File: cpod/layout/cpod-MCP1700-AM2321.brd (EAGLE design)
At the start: 15 parts, among them IC1 PCF8563DIP, Y1 32.768kHz

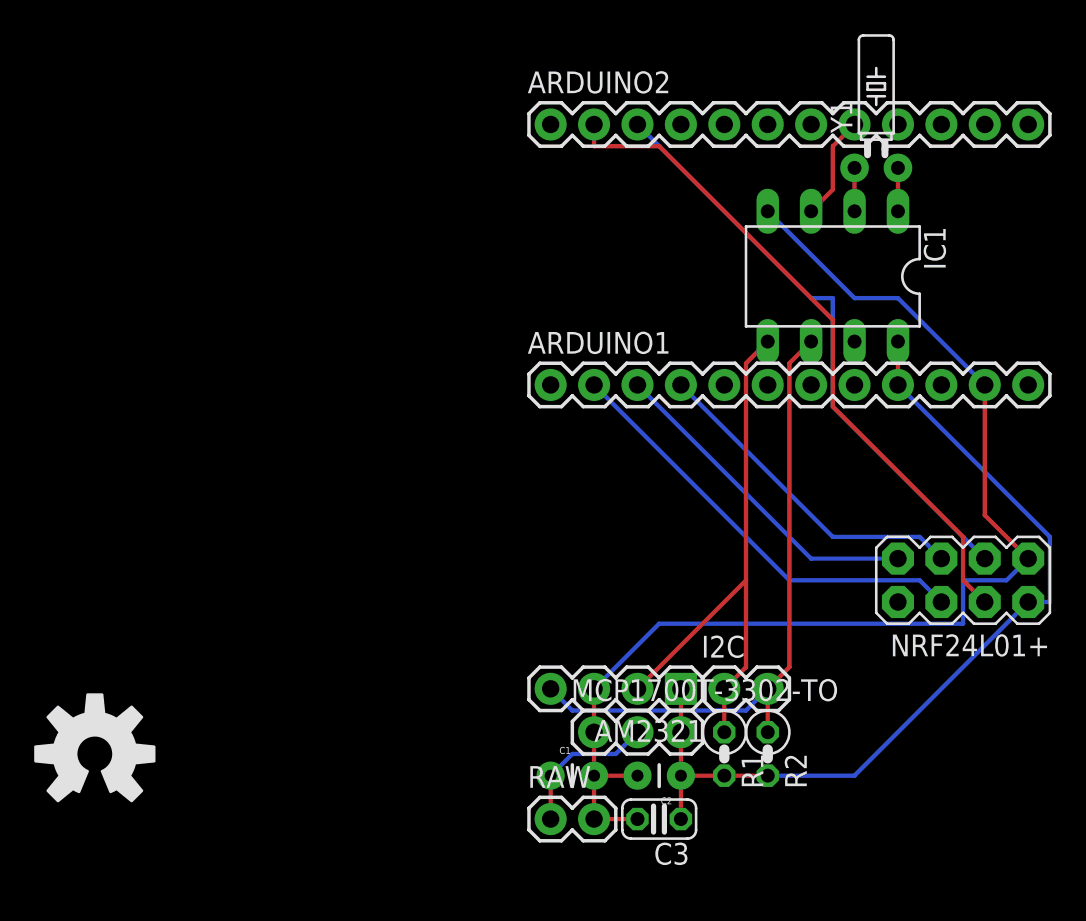
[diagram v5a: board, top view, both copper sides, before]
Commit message: 增加INT0的上拉电阻
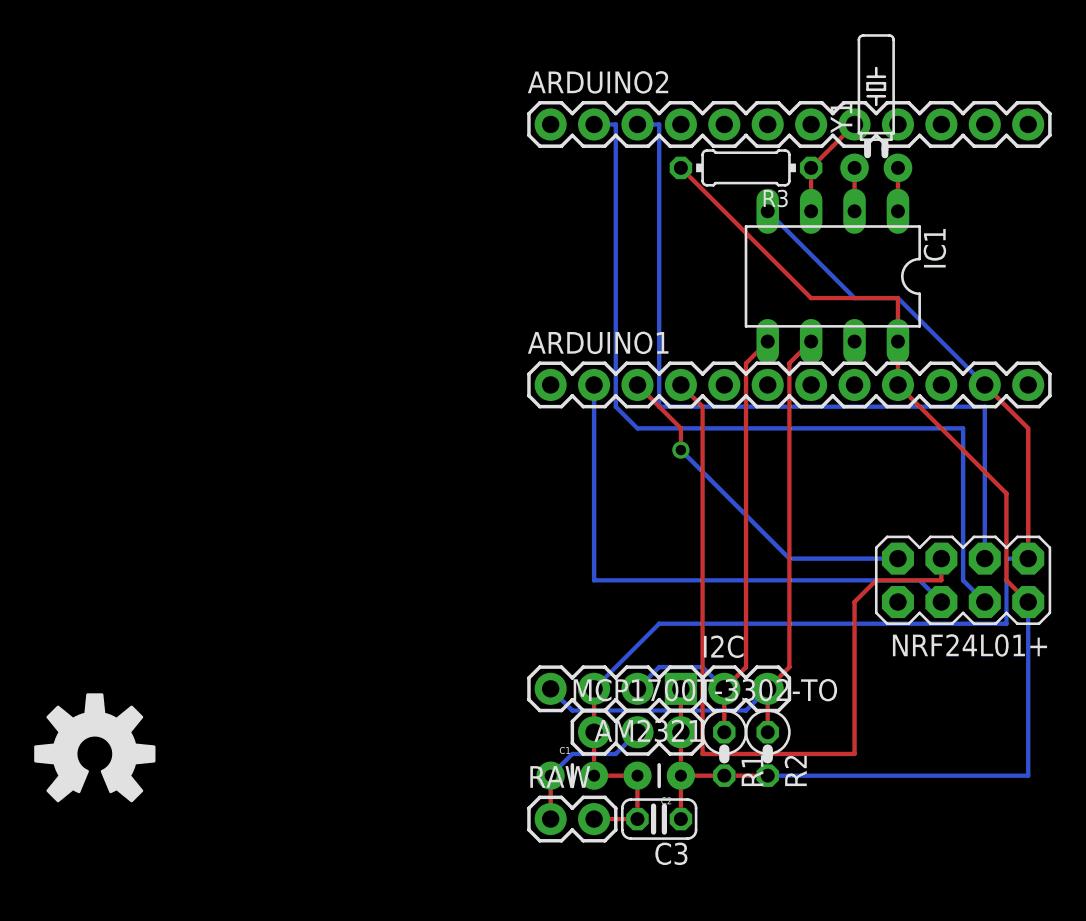
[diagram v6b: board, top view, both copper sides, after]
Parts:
- added R3: 5.1k, rcl:0204/7
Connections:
- net INT0: now also R3.1
- net VCC: now also R3.2
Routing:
- net SCK: track 19.4 -> 46.8 mm
- net VCC: track 52.3 -> 74.9 mm
- net CE: track 34.6 -> 45.7 mm
- net CSN: track 39.6 -> 49.3 mm
- net MOSI: track 25.6 -> 32.3 mm
- net SDA: track 32.9 -> 30.0 mm
- net MISO: track 19.4 -> 20.2 mm, vias 0 -> 1
- net GND: track 70.9 -> 71.6 mm
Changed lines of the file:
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@@
 <element name="Y1" library="SparkFun-FreqCtrl" package="TC26H" value="32.768kHz" x="50.8" y="-3.81"/>
 <element name="C3" library="rcl" package="C025-024X044" value="100nF" x="38.1" y="-41.91" rot="R180"/>
+<element name="R3" library="rcl" package="0204/7" value="5.1k" x="43.18" y="-3.81" rot="R180"/>
 </elements>
 <signals>
@@
 <contactref element="IC1" pad="4"/>
 <contactref element="ARDUINO1" pad="11"/>
+<contactref element="C2" pad="2"/>
+<contactref element="C3" pad="2"/>
+<wire x1="34.29" y1="-41.91" x2="36.83" y2="-41.91" width="0.254" layer="1"/>
 <wire x1="34.29" y1="-36.83" x2="34.29" y2="-39.37" width="0.254" layer="1"/>
-<wire x1="34.29" y1="-39.37" x2="34.29" y2="-41.91" width="0.254" layer="1"/>
+<wire x1="34.29" y1="-39.37" x2="36.83" y2="-39.37" width="0.254" layer="1"/>
 <wire x1="34.29" y1="-36.83" x2="34.29" y2="-34.29" width="0.254" layer="1"/>
+<wire x1="36.83" y1="-39.37" x2="36.83" y2="-41.91" width="0.254" layer="1"/>
 <wire x1="49.53" y1="-11.43" x2="44.45" y2="-6.35" width="0.254" layer="16"/>
 <wire x1="52.07" y1="-11.43" x2="49.53" y2="-11.43" width="0.254" layer="16"/>
 <wire x1="57.15" y1="-16.51" x2="52.07" y2="-11.43" width="0.254" layer="16"/>
-<wire x1="57.15" y1="-24.13" x2="59.69" y2="-26.67" width="0.254" layer="1"/>
-<wire x1="57.15" y1="-16.51" x2="57.15" y2="-24.13" width="0.254" layer="1"/>
+<wire x1="59.69" y1="-19.05" x2="59.69" y2="-26.67" width="0.254" layer="1"/>
+<wire x1="57.15" y1="-16.51" x2="59.69" y2="-19.05" width="0.254" layer="1"/>
 <wire x1="38.1" y1="-30.48" x2="34.29" y2="-34.29" width="0.254" layer="16"/>
-<wire x1="55.88" y1="-30.48" x2="38.1" y2="-30.48" width="0.254" layer="16"/>
-<wire x1="55.88" y1="-27.94" x2="55.88" y2="-30.48" width="0.254" layer="16"/>
-<wire x1="58.42" y1="-27.94" x2="55.88" y2="-27.94" width="0.254" layer="16"/>
-<wire x1="59.69" y1="-26.67" x2="58.42" y2="-27.94" width="0.254" layer="16"/>
-<contactref element="C2" pad="2"/>
-<contactref element="C3" pad="2"/>
-<wire x1="34.29" y1="-41.91" x2="36.83" y2="-41.91" width="0.254" layer="1"/>
-<wire x1="36.83" y1="-39.37" x2="34.29" y2="-39.37" width="0.254" layer="1"/>
+<wire x1="58.42" y1="-30.48" x2="38.1" y2="-30.48" width="0.254" layer="16"/>
+<wire x1="58.42" y1="-26.67" x2="58.42" y2="-30.48" width="0.254" layer="16"/>
+<wire x1="59.69" y1="-26.67" x2="58.42" y2="-26.67" width="0.254" layer="16"/>
 </signal>
 <signal name="SDA">
@@
 <wire x1="41.91" y1="-34.29" x2="41.91" y2="-36.83" width="0.254" layer="1"/>
 <wire x1="43.18" y1="-15.24" x2="44.45" y2="-13.97" width="0.254" layer="1"/>
-<wire x1="43.18" y1="-33.02" x2="43.18" y2="-27.94" width="0.254" layer="1"/>
-<wire x1="43.18" y1="-27.94" x2="43.18" y2="-15.24" width="0.254" layer="1"/>
+<wire x1="43.18" y1="-33.02" x2="43.18" y2="-15.24" width="0.254" layer="1"/>
 <wire x1="41.91" y1="-34.29" x2="43.18" y2="-33.02" width="0.254" layer="1"/>
-<wire x1="43.18" y1="-27.94" x2="36.83" y2="-34.29" width="0.254" layer="1"/>
+<wire x1="38.1" y1="-33.02" x2="36.83" y2="-34.29" width="0.254" layer="16"/>
+<wire x1="40.64" y1="-33.02" x2="38.1" y2="-33.02" width="0.254" layer="16"/>
+<wire x1="41.91" y1="-34.29" x2="40.64" y2="-33.02" width="0.254" layer="16"/>
 </signal>
 <signal name="VCC">
@@
 <contactref element="MCP1700T-3302-TO" pad="3"/>
 <contactref element="IC1" pad="8"/>
-<wire x1="39.37" y1="-34.29" x2="39.37" y2="-36.83" width="0.254" layer="1"/>
-<wire x1="52.07" y1="-16.51" x2="52.07" y2="-13.97" width="0.254" layer="1"/>
-<wire x1="41.91" y1="-39.37" x2="44.45" y2="-39.37" width="0.254" layer="1"/>
-<wire x1="49.53" y1="-39.37" x2="59.69" y2="-29.21" width="0.254" layer="16"/>
-<wire x1="44.45" y1="-39.37" x2="49.53" y2="-39.37" width="0.254" layer="16"/>
-<wire x1="60.96" y1="-25.4" x2="52.07" y2="-16.51" width="0.254" layer="16"/>
-<wire x1="60.96" y1="-29.21" x2="60.96" y2="-25.4" width="0.254" layer="16"/>
-<wire x1="59.69" y1="-29.21" x2="60.96" y2="-29.21" width="0.254" layer="16"/>
 <contactref element="C2" pad="1"/>
 <contactref element="C3" pad="1"/>
+<contactref element="R3" pad="2"/>
+<wire x1="46.99" y1="-11.43" x2="39.37" y2="-3.81" width="0.254" layer="1"/>
+<wire x1="52.07" y1="-11.43" x2="46.99" y2="-11.43" width="0.254" layer="1"/>
+<wire x1="52.07" y1="-13.97" x2="52.07" y2="-11.43" width="0.254" layer="1"/>
+<wire x1="52.07" y1="-13.97" x2="52.07" y2="-16.51" width="0.254" layer="1"/>
+<wire x1="39.37" y1="-34.29" x2="39.37" y2="-36.83" width="0.254" layer="1"/>
 <wire x1="39.37" y1="-39.37" x2="39.37" y2="-41.91" width="0.254" layer="1"/>
-<wire x1="39.37" y1="-36.83" x2="39.37" y2="-39.37" width="0.254" layer="1"/>
-<wire x1="41.91" y1="-39.37" x2="39.37" y2="-39.37" width="0.254" layer="1"/>
+<wire x1="39.37" y1="-39.37" x2="41.91" y2="-39.37" width="0.254" layer="1"/>
+<wire x1="41.91" y1="-39.37" x2="44.45" y2="-39.37" width="0.254" layer="1"/>
+<wire x1="59.69" y1="-39.37" x2="59.69" y2="-29.21" width="0.254" layer="16"/>
+<wire x1="44.45" y1="-39.37" x2="59.69" y2="-39.37" width="0.254" layer="16"/>
+<wire x1="39.37" y1="-39.37" x2="39.37" y2="-36.83" width="0.254" layer="1"/>
+<wire x1="58.42" y1="-22.86" x2="52.07" y2="-16.51" width="0.254" layer="1"/>
+<wire x1="58.42" y1="-27.94" x2="58.42" y2="-22.86" width="0.254" layer="1"/>
+<wire x1="59.69" y1="-29.21" x2="58.42" y2="-27.94" width="0.254" layer="1"/>
 </signal>
 <signal name="RAW">
@@
 <contactref element="ARDUINO1" pad="4"/>
 <contactref element="NRF24L01+" pad="5"/>
-<wire x1="48.26" y1="-25.4" x2="39.37" y2="-16.51" width="0.254" layer="16"/>
-<wire x1="53.34" y1="-25.4" x2="48.26" y2="-25.4" width="0.254" layer="16"/>
-<wire x1="54.61" y1="-26.67" x2="53.34" y2="-25.4" width="0.254" layer="16"/>
+<wire x1="40.64" y1="-17.78" x2="39.37" y2="-16.51" width="0.254" layer="1"/>
+<wire x1="40.64" y1="-38.1" x2="40.64" y2="-17.78" width="0.254" layer="1"/>
+<wire x1="49.53" y1="-38.1" x2="40.64" y2="-38.1" width="0.254" layer="1"/>
+<wire x1="49.53" y1="-29.21" x2="49.53" y2="-38.1" width="0.254" layer="1"/>
+<wire x1="50.8" y1="-27.94" x2="49.53" y2="-29.21" width="0.254" layer="1"/>
+<wire x1="54.61" y1="-27.94" x2="50.8" y2="-27.94" width="0.254" layer="1"/>
+<wire x1="54.61" y1="-26.67" x2="54.61" y2="-27.94" width="0.254" layer="1"/>
 </signal>
 <signal name="MISO">
 <contactref element="ARDUINO1" pad="3"/>
 <contactref element="NRF24L01+" pad="7"/>
-<wire x1="46.99" y1="-26.67" x2="36.83" y2="-16.51" width="0.254" layer="16"/>
-<wire x1="52.07" y1="-26.67" x2="46.99" y2="-26.67" width="0.254" layer="16"/>
+<wire x1="39.37" y1="-19.05" x2="36.83" y2="-16.51" width="0.254" layer="1"/>
+<wire x1="39.37" y1="-20.32" x2="39.37" y2="-19.05" width="0.254" layer="1"/>
+<wire x1="45.72" y1="-26.67" x2="39.37" y2="-20.32" width="0.254" layer="16"/>
+<wire x1="52.07" y1="-26.67" x2="45.72" y2="-26.67" width="0.254" layer="16"/>
+<via x="39.37" y="-20.32" extent="1-16" drill="0.6096"/>
 </signal>
 <signal name="MOSI">
 <contactref element="ARDUINO1" pad="2"/>
 <contactref element="NRF24L01+" pad="6"/>
-<wire x1="45.72" y1="-27.94" x2="34.29" y2="-16.51" width="0.254" layer="16"/>
-<wire x1="53.34" y1="-27.94" x2="45.72" y2="-27.94" width="0.254" layer="16"/>
+<wire x1="34.29" y1="-27.94" x2="34.29" y2="-16.51" width="0.254" layer="16"/>
+<wire x1="53.34" y1="-27.94" x2="34.29" y2="-27.94" width="0.254" layer="16"/>
 <wire x1="54.61" y1="-29.21" x2="53.34" y2="-27.94" width="0.254" layer="16"/>
 </signal>
@@
 <contactref element="NRF24L01+" pad="4"/>
 <contactref element="ARDUINO2" pad="2"/>
-<wire x1="55.88" y1="-27.94" x2="57.15" y2="-29.21" width="0.254" layer="1"/>
-<wire x1="55.88" y1="-25.4" x2="55.88" y2="-27.94" width="0.254" layer="1"/>
-<wire x1="48.26" y1="-17.78" x2="55.88" y2="-25.4" width="0.254" layer="1"/>
-<wire x1="48.26" y1="-12.7" x2="48.26" y2="-17.78" width="0.254" layer="1"/>
-<wire x1="38.1" y1="-2.54" x2="48.26" y2="-12.7" width="0.254" layer="1"/>
-<wire x1="34.29" y1="-2.54" x2="38.1" y2="-2.54" width="0.254" layer="1"/>
-<wire x1="34.29" y1="-1.27" x2="34.29" y2="-2.54" width="0.254" layer="1"/>
+<wire x1="55.88" y1="-27.94" x2="57.15" y2="-29.21" width="0.254" layer="16"/>
+<wire x1="55.88" y1="-19.05" x2="55.88" y2="-27.94" width="0.254" layer="16"/>
+<wire x1="36.83" y1="-19.05" x2="55.88" y2="-19.05" width="0.254" layer="16"/>
+<wire x1="35.56" y1="-17.78" x2="36.83" y2="-19.05" width="0.254" layer="16"/>
+<wire x1="35.56" y1="-1.27" x2="35.56" y2="-17.78" width="0.254" layer="16"/>
+<wire x1="34.29" y1="-1.27" x2="35.56" y2="-1.27" width="0.254" layer="16"/>
 </signal>
 <signal name="CE">
 <contactref element="NRF24L01+" pad="3"/>
 <contactref element="ARDUINO2" pad="3"/>
-<wire x1="48.26" y1="-17.78" x2="57.15" y2="-26.67" width="0.254" layer="16"/>
-<wire x1="48.26" y1="-11.43" x2="48.26" y2="-17.78" width="0.254" layer="16"/>
-<wire x1="46.99" y1="-11.43" x2="48.26" y2="-11.43" width="0.254" layer="16"/>
-<wire x1="36.83" y1="-1.27" x2="46.99" y2="-11.43" width="0.254" layer="16"/>
+<wire x1="57.15" y1="-17.78" x2="57.15" y2="-26.67" width="0.254" layer="16"/>
+<wire x1="38.1" y1="-17.78" x2="57.15" y2="-17.78" width="0.254" layer="16"/>
+<wire x1="38.1" y1="-1.27" x2="38.1" y2="-17.78" width="0.254" layer="16"/>
+<wire x1="36.83" y1="-1.27" x2="38.1" y2="-1.27" width="0.254" layer="16"/>
 </signal>
 <signal name="D9">
@@
 <contactref element="IC1" pad="3"/>
 <contactref element="ARDUINO2" pad="8"/>
-<wire x1="48.26" y1="-5.08" x2="46.99" y2="-6.35" width="0.254" layer="1"/>
-<wire x1="48.26" y1="-2.54" x2="48.26" y2="-5.08" width="0.254" layer="1"/>
-<wire x1="49.53" y1="-1.27" x2="48.26" y2="-2.54" width="0.254" layer="1"/>
+<contactref element="R3" pad="1"/>
+<wire x1="46.99" y1="-3.81" x2="46.99" y2="-6.35" width="0.254" layer="1"/>
+<wire x1="49.53" y1="-1.27" x2="46.99" y2="-3.81" width="0.254" layer="1"/>
 </signal>
 </signals>
